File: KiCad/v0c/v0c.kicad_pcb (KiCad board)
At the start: 2 copper layers, 90 x 56.8 mm, 25 parts, among them U1 AM29F160, U10 IS62C256AL, U2 74HC139, U3 74HC273, U4 74HC191, U5 74HC191, U6 74HC191, U7 74HC670, U8 74HC00, U9 IS62C256AL

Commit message: sam2695 on board
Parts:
- added C15: C_Small, Capacitor_SMD:C_0603_1608Metric_Pad1.08x0.95mm_HandSolder, F.Cu at (146.3, 113.0)
- added C16: C_Small, Capacitor_SMD:C_0603_1608Metric_Pad1.08x0.95mm_HandSolder, F.Cu at (141.0, 104.4)
- added C17: 1µF, Capacitor_SMD:C_0805_2012Metric_Pad1.18x1.45mm_HandSolder, F.Cu at (142.4, 111.2)
- added C18: C_Small, Capacitor_SMD:C_0805_2012Metric_Pad1.18x1.45mm_HandSolder, F.Cu at (144.7, 101.3)
- added C19: 1µF, Capacitor_SMD:C_0805_2012Metric_Pad1.18x1.45mm_HandSolder, F.Cu at (157.7, 108.5)
- added C2: 1µF, Capacitor_SMD:C_0805_2012Metric_Pad1.18x1.45mm_HandSolder, F.Cu at (153.8, 108.5)
- added C20: C_Small, Capacitor_SMD:C_0805_2012Metric_Pad1.18x1.45mm_HandSolder, F.Cu at (146.2, 111.2)
- added C21: C_Small, Capacitor_SMD:C_0603_1608Metric_Pad1.08x0.95mm_HandSolder, F.Cu at (141.0, 107.9)
- added R2: 100Ω, PCM_Resistor_SMD_AKL:R_0603_1608Metric_Pad1.05x0.95mm_HandSolder, F.Cu at (142.4, 114.6)
- added R3: 47KΩ, PCM_Resistor_SMD_AKL:R_0603_1608Metric_Pad1.05x0.95mm_HandSolder, F.Cu at (142.4, 113.0)
- added R4: 4.7K, PCM_Resistor_SMD_AKL:R_0603_1608Metric_Pad1.05x0.95mm_HandSolder, F.Cu at (148.8, 112.0)
- added U11: SAM2695, Package_DFN_QFN:QFN-48-1EP_6x6mm_P0.4mm_EP4.2x4.2mm, F.Cu at (148.0, 106.2)
- added U12: MCP1700, Package_TO_SOT_SMD:SOT-89-3_Handsoldering, F.Cu at (156.0, 105.0)
- added Y1: 12M, Crystal:Crystal_HC49-4H_Vertical, F.Cu at (137.4, 108.6)
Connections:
- net Net-(H1-cAUDIO) renamed /rfAUDIO
- U3 pad 16: /~{SAMCS} -> /~{SoundCS}
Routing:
- net /~{samWr}: track 0.00 -> 68.3 mm, vias 0 -> 2
- net GND: track 210.5 -> 266.7 mm, vias 69 -> 76
- net +3V3: track 0.00 -> 46.1 mm, vias 0 -> 8
- net /~{SoundCS}: track 0.00 -> 46.0 mm, vias 0 -> 2
- net /cD7: track 127.2 -> 152.5 mm, vias 1 -> 3
- net /cD5: track 106.6 -> 131.9 mm, vias 1 -> 3
- net /cD4: track 112.6 -> 137.4 mm, vias 1 -> 3
- net /cD6: track 123.0 -> 147.6 mm, vias 1 -> 3
- net /~{RESET}: track 58.4 -> 78.0 mm
- net /cA0: track 139.0 -> 151.5 mm, vias 3 -> 4
- net VCC: track 459.6 -> 469.4 mm, vias 19 -> 20
- net Net-(U11-X2): track 0.00 -> 9.72 mm
- net /cA1: track 115.9 -> 124.1 mm
- net Net-(U11-X1): track 0.00 -> 8.10 mm
- net /R~{W}: track 86.4 -> 80.1 mm
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
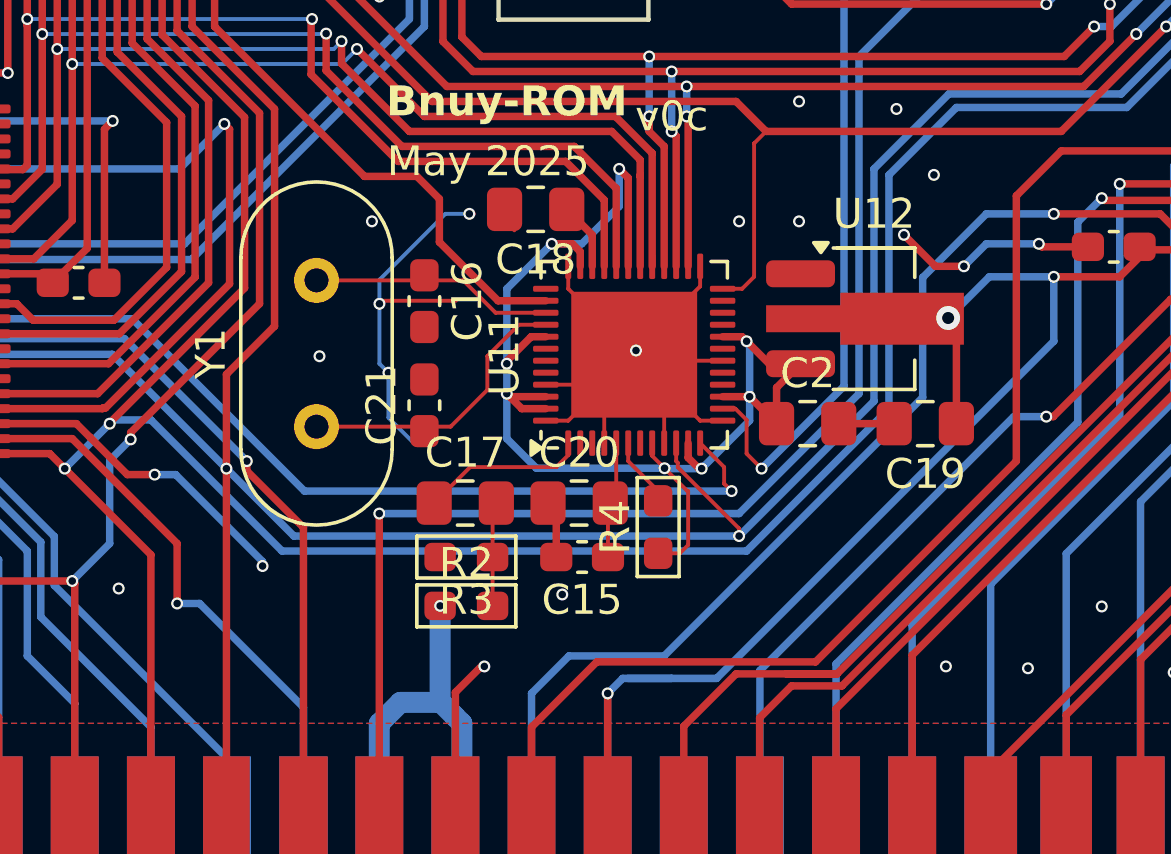
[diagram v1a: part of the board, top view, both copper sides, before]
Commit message: Silkscreen and schematic tweaks
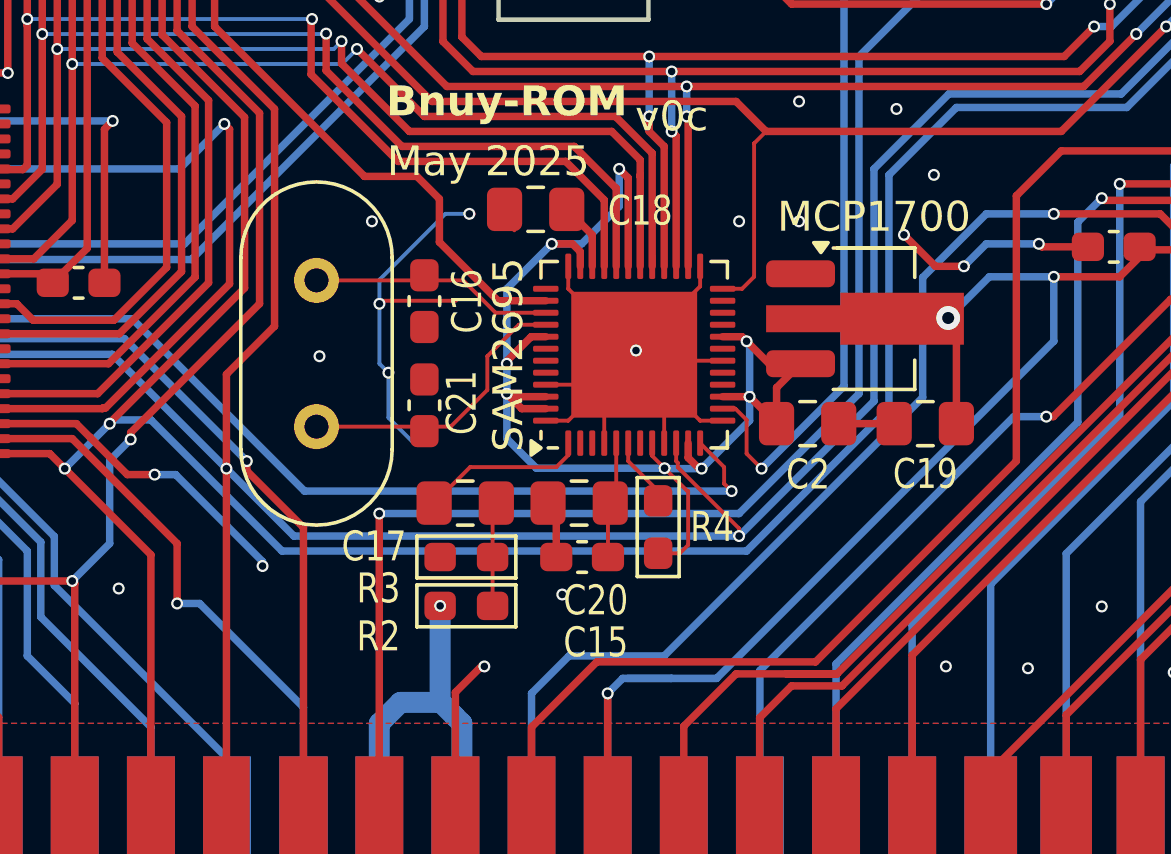
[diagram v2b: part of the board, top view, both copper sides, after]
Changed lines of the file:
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@@
 		(tags "capacitor handsolder")
 		(property "Reference" "C15"
-			(at 0 -1.43 0)
+			(at -1.5375 -2.85 0)
 			(layer "F.SilkS")
 			(effects
 				(font
-					(size 1 1)
+					(size 1 0.8)
 					(thickness 0.15)
 				)
+				(justify right)
 			)
 		)
@@
 		(tags "capacitor handsolder")
 		(property "Reference" "C2"
-			(at 0 -1.68 0)
+			(at 0.0125 1.7 0)
 			(layer "F.SilkS")
 			(effects
 				(font
-					(size 1 1)
+					(size 1 0.8)
 					(thickness 0.15)
 				)
@@
 			(at 0 -3.5 0)
 			(layer "F.SilkS")
+			(hide yes)
 			(effects
 				(font
@@
 		)
 		(property "Value" "MCP1700"
-			(at 0 3.5 0)
-			(layer "F.Fab")
+			(at 0 -3.4 0)
+			(layer "F.SilkS")
 			(effects
 				(font
@@
 		(tags "resistor handsolder")
 		(property "Reference" "R3"
-			(at 0 -1.43 0)
+			(at 2.2 -1.05 0)
 			(layer "F.SilkS")
 			(effects
 				(font
-					(size 1 1)
+					(size 1 0.8)
 					(thickness 0.15)
 				)
+				(justify right)
 			)
 		)
@@
 		(tags "resistor handsolder")
 		(property "Reference" "R4"
-			(at 0 -1.43 90)
+			(at 0 1.8 180)
 			(layer "F.SilkS")
 			(effects
 				(font
-					(size 1 1)
+					(size 1 0.8)
 					(thickness 0.15)
 				)
@@
 		(tags "capacitor handsolder")
 		(property "Reference" "C17"
-			(at 0 -1.68 0)
+			(at -1.9625 1.45 0)
 			(layer "F.SilkS")
 			(effects
 				(font
-					(size 1 1)
+					(size 1 0.8)
 					(thickness 0.15)
 				)
+				(justify right)
 			)
 		)
@@
 		(tags "capacitor handsolder")
 		(property "Reference" "C18"
-			(at 0 -1.68 0)
+			(at -3.4875 -0.05 0)
 			(layer "F.SilkS")
 			(effects
 				(font
-					(size 1 1)
+					(size 1 0.8)
 					(thickness 0.15)
 				)
@@
 		(tags "capacitor handsolder")
 		(property "Reference" "C20"
-			(at 0 -1.68 0)
+			(at 1.6375 3.25 0)
 			(layer "F.SilkS")
 			(effects
 				(font
-					(size 1 1)
+					(size 1 0.8)
 					(thickness 0.15)
 				)
+				(justify right)
 			)
 		)
@@
 			(at 2.44 -3.525 90)
 			(layer "F.SilkS")
+			(hide yes)
 			(effects
 				(font
@@
 			(effects
 				(font
-					(size 1 1)
+					(size 1 0.8)
 					(thickness 0.15)
 				)
@@
 			(at 0 -4.33 90)
 			(layer "F.SilkS")
+			(hide yes)
 			(effects
 				(font
@@
 		)
 		(property "Value" "SAM2695"
-			(at 0 4.33 90)
-			(layer "F.Fab")
+			(at 0 -4.2 90)
+			(layer "F.SilkS")
 			(effects
 				(font
@@
 		(tags "capacitor handsolder")
 		(property "Reference" "C21"
-			(at 0 -1.43 90)
+			(at 0.0875 1.25 90)
 			(layer "F.SilkS")
 			(effects
 				(font
-					(size 1 1)
+					(size 1 0.8)
 					(thickness 0.15)
 				)
@@
 		(tags "resistor handsolder")
 		(property "Reference" "R2"
-			(at 0 -1.43 0)
+			(at -2.2 1.02 0)
 			(layer "F.SilkS")
 			(effects
 				(font
-					(size 1 1)
+					(size 1 0.8)
 					(thickness 0.15)
 				)
+				(justify right)
 			)
 		)
@@
 			(effects
 				(font
-					(size 1 1)
+					(size 1 0.8)
 					(thickness 0.15)
 				)

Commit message: Change Scanline Circuit
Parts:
- U4: value 74HC191 -> 4520
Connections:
- R2 pad 1: /rfAUDIO -> /Sound/rfAUDIO
- U11 pad 10: /cA0 -> /Sound/cA0
- U11 pad 12: /~{samWr} -> /Sound/~{samWr}
- U11 pad 14: /~{SoundCS} -> /Sound/~{SoundCS}
- U11 pad 24: /cD0 -> /Sound/cD0
- U11 pad 26: /cD1 -> /Sound/cD1
- U11 pad 27: /cD2 -> /Sound/cD2
- U11 pad 28: /cD3 -> /Sound/cD3
- U11 pad 29: /cD4 -> /Sound/cD4
- U11 pad 30: /cD5 -> /Sound/cD5
- U11 pad 32: /cD6 -> /Sound/cD6
- U11 pad 33: /cD7 -> /Sound/cD7
- U11 pad 38: /~{RESET} -> /Sound/~{RESET}
- U4 pad 10: GND -> /~{pRD}
- U4 pad 11: /~{irqWr} -> Net-(U4A-Reset)
- U4 pad 14: /pA12 -> unconnected-(U4B-Q4-Pad14)
- U4 pad 15: GND -> /pA13
- U4 pad 2: unconnected-(U4-Q1-Pad2) -> /~{pRD}
- U4 pad 4: /~{IRQRun} -> unconnected-(U4A-Q2-Pad4)
- U4 pad 5: VCC -> /ScanlineClk
- U4 pad 6: Net-(U4-Q2) -> unconnected-(U4A-Q4-Pad6)
- U4 pad 7: unconnected-(U4-Q3-Pad7) -> Net-(U4A-Reset)
- U4 pad 9: GND -> Net-(U4A-Reset)
- U5 pad 14: Net-(U4-Q2) -> /ScanlineClk
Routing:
- net /~{pRD}: track 41.7 -> 81.6 mm, vias 0 -> 2
- net /ScanlineClk: track 0.00 -> 37.5 mm, vias 0 -> 2
- net Net-(U4-Q2): track 36.2 -> 0.00 mm, vias 2 -> 0
- net /pA13: track 44.4 -> 74.0 mm, vias 1 -> 2
- net /pA12: track 70.8 -> 46.5 mm
- net GND: track 266.7 -> 282.3 mm, vias 76 -> 77
- net VCC: track 469.4 -> 454.1 mm, vias 20 -> 19
- net /~{irqWr}: track 126.6 -> 113.1 mm, vias 8 -> 6
- net /~{IRQRun}: track 71.2 -> 60.4 mm, vias 6 -> 4
- net Net-(U4A-Reset): track 0.00 -> 8.70 mm

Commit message: Update pcbs and readme
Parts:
- removed C12: C_Small, Capacitor_SMD:C_0603_1608Metric_Pad1.08x0.95mm_HandSolder
- removed U5, U6: 74HC191, Package_SO:SOIC-16_3.9x9.9mm_P1.27mm
- added U13: 74HC40103, Package_SO:SOIC-16_3.9x9.9mm_P1.27mm, F.Cu at (167.3, 85.2)
- U4: value 4520 -> 74HC4520
- moved C9 6.88 mm to (170.6, 79.0), turned to 180 degrees
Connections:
- net /cA1 renamed cA1
- net /cA10 renamed cA10
- net /cA11 renamed cA11
- net /cA12 renamed cA12
- net /cA13 renamed cA13
- net /cA14 renamed cA14
- net /cA2 renamed cA2
- net /cA3 renamed cA3
- net /cA4 renamed cA4
- net /cA5 renamed cA5
- net /cA6 renamed cA6
- net /cA7 renamed cA7
- net /cA8 renamed cA8
- net /cA9 renamed cA9
- C1 pad 1: /~{RESET} -> ~{RESET}
- D1 pad 1: /~{RESET} -> ~{RESET}
- H1 pad 13: /cA0 -> cA0
- H1 pad 36: /cD7 -> cD7
- H1 pad 37: /cD6 -> cD6
- H1 pad 38: /cD5 -> cD5
- H1 pad 39: /cD4 -> cD4
- H1 pad 40: /cD3 -> cD3
- H1 pad 41: /cD2 -> cD2
- H1 pad 42: /cD1 -> cD1
- H1 pad 43: /cD0 -> cD0
- H1 pad 45: /rfAUDIO -> rfAudio
- H1 pad 46: /rfAUDIO -> rfAudio
- R1 pad 2: /~{RESET} -> ~{RESET}
- R2 pad 1: /Sound/rfAUDIO -> rfAudio
- U1 pad 12: /~{RESET} -> ~{RESET}
- U1 pad 29: /cD0 -> cD0
- U1 pad 31: /cD1 -> cD1
- U1 pad 33: /cD2 -> cD2
- U1 pad 35: /cD3 -> cD3
- U1 pad 38: /cD4 -> cD4
- U1 pad 40: /cD5 -> cD5
- U1 pad 42: /cD6 -> cD6
- U1 pad 44: /cD7 -> cD7
- U1 pad 45: /cA0 -> cA0
- U10 pad 10: /cA0 -> cA0
- U10 pad 11: /cD0 -> cD0
- U10 pad 12: /cD1 -> cD1
- U10 pad 13: /cD2 -> cD2
- U10 pad 15: /cD3 -> cD3
- U10 pad 16: /cD4 -> cD4
- U10 pad 17: /cD5 -> cD5
- U10 pad 18: /cD6 -> cD6
- U10 pad 19: /cD7 -> cD7
- U11 pad 10: /Sound/cA0 -> cA0
- U11 pad 12: /Sound/~{samWr} -> ~{samWr}
- U11 pad 14: /Sound/~{SoundCS} -> ~{SoundCS}
- U11 pad 24: /Sound/cD0 -> cD0
- U11 pad 26: /Sound/cD1 -> cD1
- U11 pad 27: /Sound/cD2 -> cD2
- U11 pad 28: /Sound/cD3 -> cD3
- U11 pad 29: /Sound/cD4 -> cD4
- U11 pad 30: /Sound/cD5 -> cD5
- U11 pad 32: /Sound/cD6 -> cD6
- U11 pad 33: /Sound/cD7 -> cD7
- U11 pad 38: /Sound/~{RESET} -> ~{RESET}
- U2 pad 11: /~{samWr} -> ~{samWr}
- U3 pad 1: /~{RESET} -> ~{RESET}
- U3 pad 13: /cD4 -> cD4
- U3 pad 14: /cD5 -> cD5
- U3 pad 16: /~{SoundCS} -> ~{SoundCS}
- U3 pad 17: /cD6 -> cD6
- U3 pad 18: /cD7 -> cD7
- U3 pad 3: /cD0 -> cD0
- U3 pad 4: /cD1 -> cD1
- U3 pad 7: /cD2 -> cD2
- U3 pad 8: /cD3 -> cD3
- U7 pad 1: /cD1 -> cD1
- U7 pad 14: /cA0 -> cA0
- U7 pad 15: /cD0 -> cD0
- U7 pad 2: /cD2 -> cD2
- U7 pad 3: /cD3 -> cD3
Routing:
- net cD0: track 0.00 -> 160.5 mm, vias 0 -> 4
- net /cD7: track 152.5 -> 0.00 mm, vias 3 -> 0
- net cD3: track 0.00 -> 152.4 mm, vias 0 -> 5
- net cA0: track 0.00 -> 151.5 mm, vias 0 -> 4
- net /cA0: track 151.5 -> 0.00 mm, vias 4 -> 0
- net cD2: track 0.00 -> 150.6 mm, vias 0 -> 5
- net cD7: track 0.00 -> 149.1 mm, vias 0 -> 3
- net cD4: track 0.00 -> 148.9 mm, vias 0 -> 3
- net /cD1: track 148.8 -> 0.00 mm, vias 5 -> 0
- net /cD0: track 148.8 -> 0.00 mm, vias 3 -> 0
- net cD5: track 0.00 -> 148.5 mm, vias 0 -> 3
- net cD1: track 0.00 -> 148.4 mm, vias 0 -> 6
- net /cD6: track 147.6 -> 0.00 mm, vias 3 -> 0
- net cD6: track 0.00 -> 147.0 mm, vias 0 -> 3
- net /cD3: track 146.8 -> 0.00 mm, vias 5 -> 0
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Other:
- board text added: "July 2025"
- board text added: "irq count"
- board text removed: "May 2025"
- board text removed: "irq hi"
- board text removed: "irq lo"
